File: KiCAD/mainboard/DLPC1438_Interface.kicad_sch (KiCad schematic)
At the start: 38 parts, among them J2 Conn_01x07_Pin, J31 Conn_01x08_Pin, J7 Conn_01x05_Pin, J9 Conn_01x09_Pin, U1 TXS0102DCU

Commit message: commiting progress hope this doesn't crash
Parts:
- added C1, C112, C114: 100nF, Capacitor_SMD:C_0805_2012Metric_Pad1.18x1.45mm_HandSolder, symbol Device:C
- added IC3, IC4, IC5, IC6, IC7, IC8, U14, U5: SN74AUP1G06DCKR, tp_library:SOT65P210X110-5N, symbol tp_library:SN74AUP1G06DCKR
- added J2: Conn_01x07_Pin, Connector_PinHeader_2.54mm:PinHeader_1x07_P2.54mm_Vertical, symbol Connector:Conn_01x07_Pin
- added J3: Conn_02x05_Odd_Even, Connector_PinHeader_2.54mm:PinHeader_2x05_P2.54mm_Vertical, symbol Connector_Generic:Conn_02x05_Odd_Even
- added J31: Conn_01x08_Pin, Connector_PinHeader_2.54mm:PinHeader_1x08_P2.54mm_Vertical, symbol Connector:Conn_01x08_Pin
- added J4: Conn_01x05_Pin, Connector_PinHeader_2.54mm:PinHeader_1x05_P2.54mm_Vertical, symbol Connector:Conn_01x05_Pin
- added R164, R170, R2: 10k, Resistor_SMD:R_0805_2012Metric_Pad1.20x1.40mm_HandSolder, symbol Device:R_US
- added R166: 10k, Resistor_SMD:R_0402_1005Metric, symbol Device:R_US
- added R3, R5: 100, Resistor_SMD:R_0805_2012Metric_Pad1.20x1.40mm_HandSolder, symbol Device:R_US
- added TP3: TestPoint, symbol Connector:TestPoint
- added U12: ECS-2520MV-xxx-xx, Oscillator:Oscillator_SMD_ECS_2520MV-xxx-xx-4Pin_2.5x2.0mm, symbol Oscillator:ECS-2520MV-xxx-xx
- added U13: MX25L3233FM2, Package_SO:SOIC-8_5.3x5.3mm_P1.27mm, symbol Memory_Flash:MX25L3233FM2
- added U22: TXS0102DCU, Package_SO:VSSOP-8_2.3x2mm_P0.5mm, symbol Logic_LevelTranslator:TXS0102DCU
- gave numbers to parts that had none: 7
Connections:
- net P1P8V_DLPC is gone; now on net GND: R177.2
- net VCC is gone; now on net GND: C121.1, C129.1, C133.1, C134.1, C144.1, C145.1, C156.1, C157.1, IC?.C4 (VSS_1), IC?.C6 (VSS_2), IC?.C7 (VCC_1), IC?.C8 (VSS_3), IC?.C9 (VCC_2), IC?.D10 (VSS_6), IC?.D4 (VCC_3), IC?.D6 (VSS_4), IC?.D8 (VSS_5), IC?.E12 (VCC_4), IC?.E13 (VSS_8), IC?.E4 (VSS_7), IC?.F12 (VCC_5), IC?.F4 (VSS_9), IC?.G10 (VSS_20), IC?.G12 (VSS_21), IC?.G13 (VSS_22), IC?.G4 (VSS_15), IC?.G6 (VSS_16), IC?.G7 (VSS_17), IC?.G8 (VSS_18), IC?.G9 (VSS_19), IC?.H10 (VSS_28), IC?.H12 (VSS_29), IC?.H4 (VSS_23), IC?.H6 (VSS_24), IC?.H7 (VSS_25), IC?.H8 (VSS_26), IC?.H9 (VSS_27), IC?.J13 (VSS_36), IC?.J3 (VSS_30), IC?.K10 (VSS_42), IC?.K12 (VSS_43), IC?.K13 (VCC_6), IC?.K4 (VSS_37), IC?.K6 (VSS_38), IC?.K7 (VSS_39), IC?.K8 (VSS_40), IC?.K9 (VSS_41), IC?.L3 (VSS_44), IC?.M12 (VSS_48), IC?.M3 (VCC_INTF_1), IC?.M4 (VSS_45), IC?.M5 (VSS_46), IC?.M7 (VCC_INTF_2), IC?.M8 (VSS_47), IC?.N3 (VCC_INTF_3), IC?.N7 (VCC_INTF_4)
- net VDDLP12 is gone; now on net P1P1V: C127.1, IC?.C3 (VDDLP12)
- net GND: now also C112.1, C112.2, C114.1, C114.2, J2.1 (Pin_1), J2.2 (Pin_2), J4.1 (Pin_1), R164.2, R166.1, TP3.1, U14.3 (GND), U14.5 (VCC), U5.3 (GND), U5.5 (VCC)
- net JTAG_TMS: now reaches IC?.M13 (JTAGTMS1)
- net JTAG_TMS: now also J2.6 (Pin_6)
- net JTAG_TDO: now reaches IC?.N13 (JTAGTDO1)
- net JTAG_TDO: now also J2.4 (Pin_4)
- net TSTPT_6: now reaches IC?.N14 (TSTPT_6)
- net TSTPT_6: now also J31.7 (Pin_7)
- net TSTPT_7: now reaches IC?.N15 (TSTPT_7)
- net TSTPT_7: now also J31.8 (Pin_8)
- net DLPC_HOST_IRQ: now reaches IC?.N8 (HOST_IRQ)
- net DLPC_HOST_IRQ: now also R166.2, U14.2 (A), U5.2 (A)
- net JTAG_TRSTZ: now reaches IC?.P11 (JTAGTRSTZ)
- net JTAG_TRSTZ: now also J2.7 (Pin_7), R164.1
- net at IC?.P12 (JTAGTCK): no longer names the net of IC?.P12 (JTAGTCK)
- net at IC?.P12 (JTAGTCK): now also J2.3 (Pin_3)
- net JTAG_TDI: now reaches IC?.P13 (JTAGTDI)
- net JTAG_TDI: now also J2.5 (Pin_5)
- net TSTPT_4: now reaches IC?.P14 (TSTPT_4)
- net TSTPT_4: now also J31.5 (Pin_5)
- net TSTPT_5: now reaches IC?.P15 (TSTPT_5)
- net TSTPT_5: now also J31.6 (Pin_6)
- net TSTPT_0: now reaches IC?.R12 (TSTPT_0)
- net TSTPT_0: now also J31.1 (Pin_1)
- net TSTPT_1: now reaches IC?.R13 (TSTPT_1)
- net TSTPT_1: now also J31.2 (Pin_2)
- net TSTPT_2: now reaches IC?.R14 (TSTPT_2)
- net TSTPT_2: now also J31.3 (Pin_3)
- net TSTPT_3: now reaches IC?.R15 (TSTPT_3)
- net TSTPT_3: now also J31.4 (Pin_4)
- net VDD renamed P1P1V
- new net: R5.1, U5.4 (Y)
- new net HOST_IR: R170.1, U14.4 (Y)
- new net P3P3V: R170.2
- new net SPI0_CLK: J4.5 (Pin_5)
- new net SPI0_CSz0: J4.4 (Pin_4)
- new net SPI0_MISO: J4.2 (Pin_2)
- new net SPI0_MOSI: J4.3 (Pin_3)
- no-connect marks 11 -> 13
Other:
- moved on the sheet: U1

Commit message: DLPC pins all connected to pin, some circutry incomplete inclding LEDs, SPI, Crystal Ocillator, and DLPC programming flash. I also need to import a symbol and footprint for the ferrite beads, and some of the passive components I realized had the wrong package size 0403 instead of 0805.
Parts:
- added C170, C171: 100nF, Capacitor_SMD:C_0805_2012Metric_Pad1.18x1.45mm_HandSolder, symbol Device:C
- added R53, R54, R55, R73: 3.3k, Resistor_SMD:R_0805_2012Metric_Pad1.20x1.40mm_HandSolder, symbol Device:R_US
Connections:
- net GND: now also IC?.C10 (HWTEST_E_N), IC?.M11 (VCC_7), IC?.P10 (PDATA_23), IC?.P4 (PDATA_11), IC?.P5 (PDATA_13), IC?.P6 (PDATA_15), IC?.P7 (PDATA_17), IC?.P8 (PDATA_19), IC?.P9 (PDATA_21), U22.2 (GND), U22.3 (VCCA), C170.1, C170.2, C171.2, R53.2, R54.2, R55.2, R73.2
- net P3P3V: now also U22.7 (VCCB), C171.1
- net CMP_OUT: now reaches IC?.A12 (CMP_OUT)
- net DLPC_SPICLK: now reaches IC?.A13 (SPI0_CLK)
- net DLPC_SPICSZ0: now reaches IC?.A14 (SPI0_CSZ0)
- net DLPC_SPIDOUT: now reaches IC?.B12 (SPI0_DIN)
- net SPI_MISO: now reaches IC?.B13 (SPI0_DOUT)
- net DLPC_LED_SEL_1: now reaches IC?.B14 (LED_SEL_1)
- net DLPC_LED_SEL_0: now reaches IC?.B15 (LED_SEL_0)
- net RESETZ: now reaches IC?.C11 (RESETZ)
- net INTZ: now reaches IC?.C13 (PARKZ)
- net P3P3V_SB: now reaches C138.1, IC?.D11 (VCC_FLSH)
- net OSC_OUT: now reaches IC?.H1 (PLL_REFCL_K_I)
- net DLPC_PLLO: now reaches IC?.J1 (PLL_REFCL_K_O)
- net IIC1_SCL: now reaches IC?.N10 (IIC0_SCL)
- net IIC1_SCL: now also U22.8 (B1), R73.1
- net IIC1_SDA: now reaches IC?.N9 (IIC0_SDA)
- net IIC1_SDA: now also U22.1 (B2), R53.1
- net IIC1_SDA_1p8: now reaches IC?.R10 (IIC1_SDA)
- net IIC1_SDA_1p8: now also U22.4 (A2), R54.1
- net IIC0_SCL_1p8: now reaches IC?.R11 (IIC1_SCL)
- net IIC0_SCL_1p8: now also U22.5 (A1), R55.1
- no-connect marks 13 -> 15
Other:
- moved on the sheet: C1, C112, J2, J3, J31, R164, R2, R3, U12, U13, U22

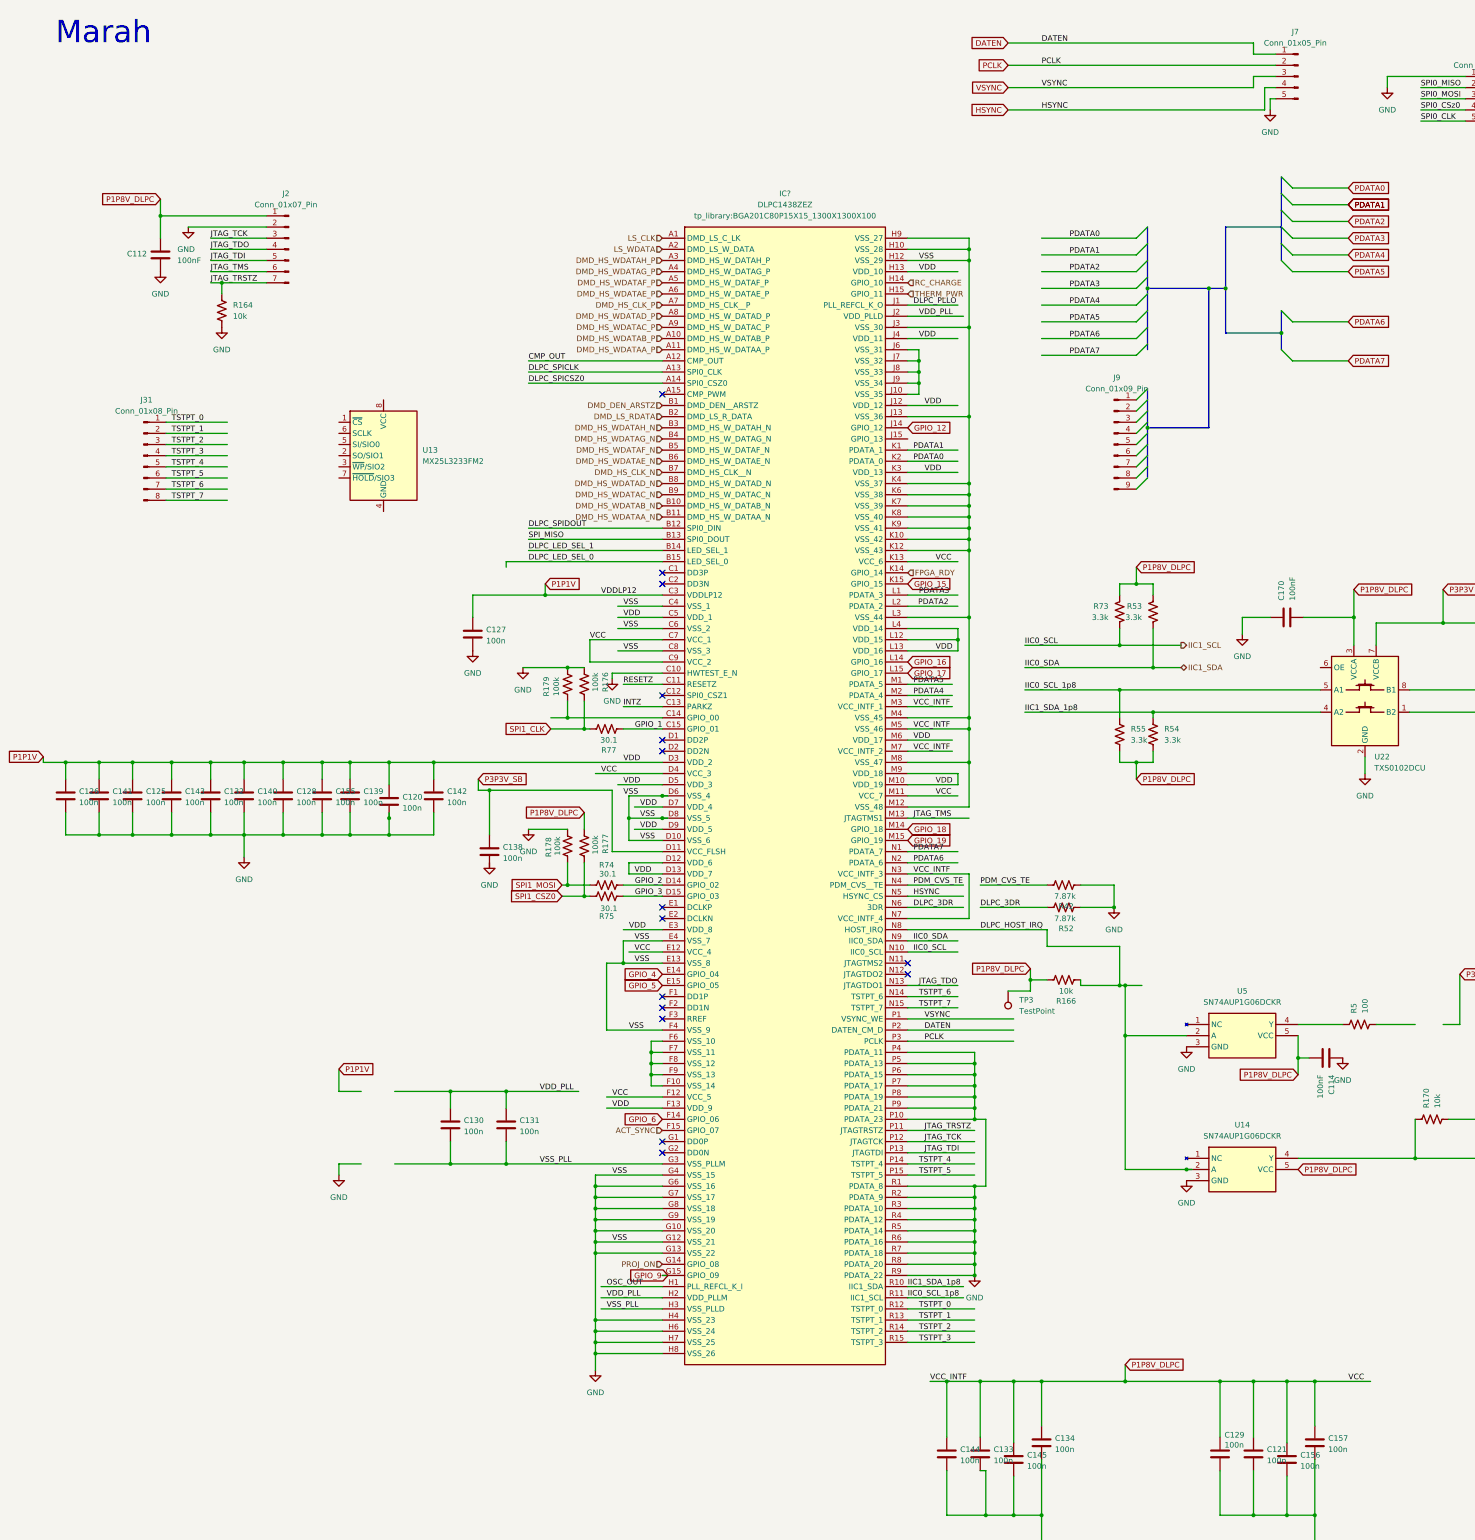
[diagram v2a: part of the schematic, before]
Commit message: Changed all FPGA Connections to what we want, created a new project for the connection board
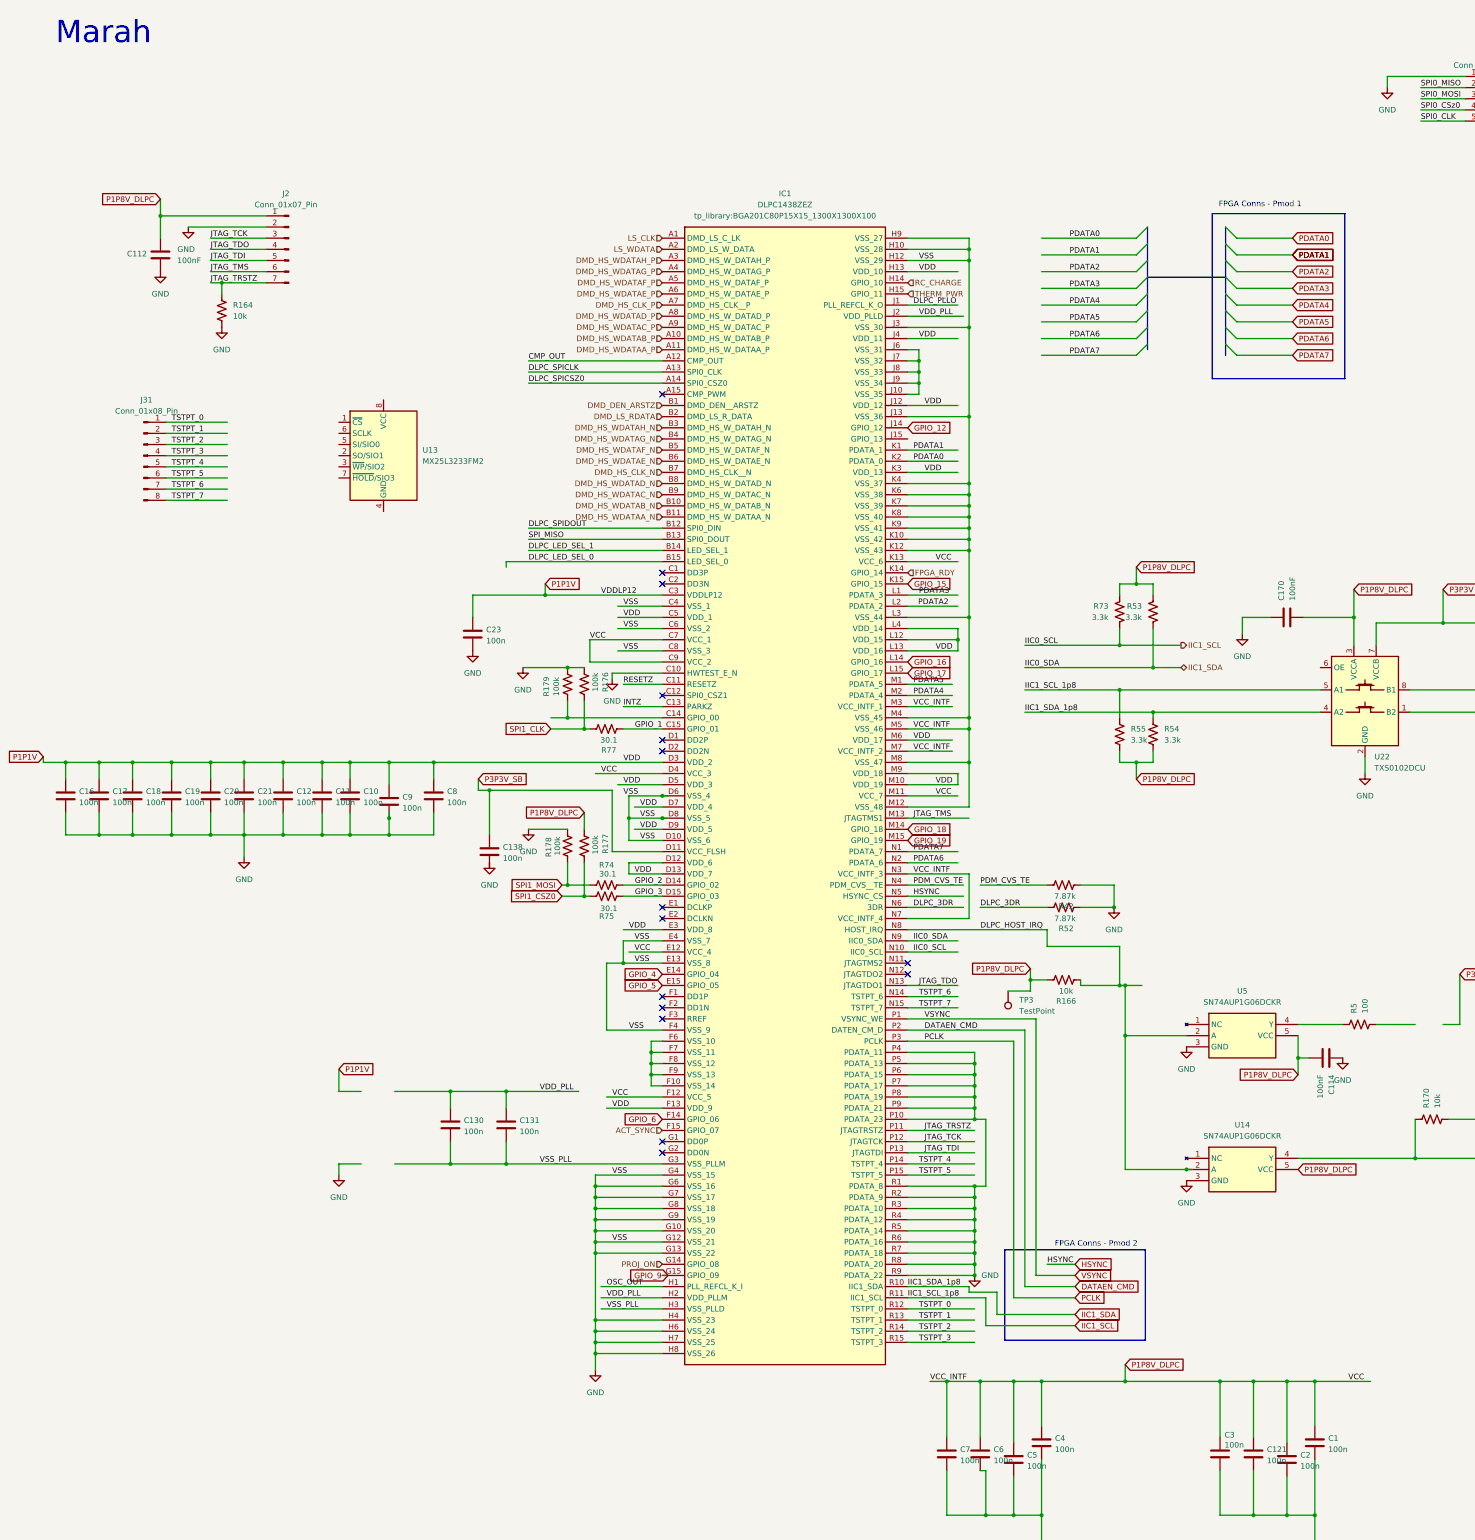
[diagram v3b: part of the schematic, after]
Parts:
- removed J7: Conn_01x05_Pin, Connector_PinHeader_2.54mm:PinHeader_1x05_P2.54mm_Vertical, symbol Connector:Conn_01x05_Pin
- removed J9: Conn_01x09_Pin, Connector_PinHeader_2.54mm:PinHeader_1x09_P2.54mm_Vertical, symbol Connector:Conn_01x09_Pin
- gave numbers to parts that had none: 1
- renumbered C157 to C1, C139 to C10, C155 to C11, C128 to C12, C126 to C16, C141 to C17, C125 to C18, C143 to C19, C156 to C2, C132 to C20, C140 to C21, C127 to C23, C129 to C3, C134 to C4, C145 to C5, C133 to C6, C144 to C7, C142 to C8, C120 to C9
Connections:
- net IIC0_SCL_1p8 is gone; now on net IIC1_SCL: IC1.R11 (IIC1_SCL), R55.1, U22.5 (A1)
- net IIC1_SDA_1p8 is gone; now on net IIC1_SDA: IC1.R10 (IIC1_SDA), R54.1, U22.4 (A2)
- net DATEN renamed DATAEN_CMD
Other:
- note added: "FPGA Conns - Pmod 1"
- note added: "FPGA Conns - Pmod 2"

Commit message: SPI and prog connection
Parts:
- added C115, C7: 100nF, Capacitor_SMD:C_0805_2012Metric_Pad1.18x1.45mm_HandSolder, symbol Device:C
- added J7: Conn_01x05_Pin, Connector_PinHeader_2.54mm:PinHeader_1x05_P2.54mm_Vertical, symbol Connector:Conn_01x05_Pin
- added R1, R172, R173, R18, R43, R7, R76: 30.1, Resistor_SMD:R_0805_2012Metric_Pad1.20x1.40mm_HandSolder, symbol Device:R_US
- added R16: 0, Resistor_SMD:R_0805_2012Metric_Pad1.20x1.40mm_HandSolder, symbol Device:R_US
- added R163, R165: 10k, Resistor_SMD:R_0805_2012Metric_Pad1.20x1.40mm_HandSolder, symbol Device:R_US
- added R168, R17, R19, R4: 100k, Resistor_SMD:R_0805_2012Metric_Pad1.20x1.40mm_HandSolder, symbol Device:R_US
- renumbered C9 to C120, C18 to C125, C16 to C126, C23 to C127, C12 to C128, C3 to C129, C20 to C132, C6 to C133, C4 to C134, C10 to C139, C21 to C140, C17 to C141, C8 to C142, C19 to C143, C7 to C144, C5 to C145, C11 to C155, C2 to C156, C1 to C157, IC1 to IC?
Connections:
- net SPI_MISO is gone; now on net DLPC_SPIDOUT: IC?.B13 (SPI0_DOUT)
- net DATAEN_CMD: no longer IC?.P2 (DATEN_CM_D)
- net DLPC_SPICLK: now also R172.2
- net DLPC_SPICSZ0: now also R76.2
- net DLPC_SPIDOUT: now also R173.2; no longer IC?.B12 (SPI0_DIN)
- net GND: now also J3.10 (Pin_10), J3.2 (Pin_2), U12.2 (GND), U13.4 (GND), C115.2, C7.2, J7.5 (Pin_5), R16.2, R165.2, R168.1, R19.2
- net HSYNC: now also J7.4 (Pin_4)
- net IIC1_SCL: no longer IC?.R11 (IIC1_SCL), R55.1, U22.5 (A1)
- net IIC1_SDA: no longer IC?.R10 (IIC1_SDA), R54.1, U22.4 (A2)
- net OSC_OUT: now also R43.2
- net P3P3V_SB: now also U13.3 (~{WP}/SIO2), U13.7 (~{HOLD}/SIO3), U13.8 (VCC), C115.1, R17.1
- net PCLK: now also J7.2 (Pin_2)
- net SPI0_CLK: now also J3.7 (Pin_7), U13.6 (SCLK), R172.1, R19.1
- net SPI0_MISO: now also IC?.B12 (SPI0_DIN), J3.5 (Pin_5), R168.2, R18.1
- net SPI0_MOSI: now also U13.5 (SI/SIO0), R173.1
- net VSYNC: now also J7.3 (Pin_3)
- net SPI0_CSZ0: now reaches U13.1 (~{CS})
- net SPI0_CSZ0: now also J3.9 (Pin_9), R17.2, R76.1
- net SPI0_MISO_T: now reaches U13.2 (SO/SIO1)
- net SPI0_MISO_T: now also R18.2
- net VOSC: now reaches U12.1 (Tri-State)
- net VOSC: now also U12.4 (VDD), C7.1, R16.1
- net OSC_OUT_T: now reaches U12.3 (OUT)
- net OSC_OUT_T: now also R43.1
- net SPI0_5V: now reaches J3.4 (Pin_4)
- net SPI0_5V: now also R163.1
- new net DATEN: J7.1 (Pin_1)
- new net DATEN_CMD: IC?.P2 (DATEN_CM_D)
- new net DLPC_FLSH_PROG: R163.2, R165.1
- new net IIC1_SCL_1p8: IC?.R11 (IIC1_SCL), R55.1, U22.5 (A1)
- new net IIC1_SDA_1p8: IC?.R10 (IIC1_SDA), R54.1, U22.4 (A2)
- no-connect marks 15 -> 17
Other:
- moved on the sheet: C114, C120, C125, C126, C128, C132, C139, C140, C141, C142, C143, C155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
